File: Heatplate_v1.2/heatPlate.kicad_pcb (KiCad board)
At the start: 2 copper layers, 112 x 180 mm, 62 parts, among them J1 Conn_01x02, J3 TYPE-C-31-M-12, Q1 SS8050, Q2 IRLR8726TRPBF, SW1 SW_Push, SW2 SW_Push, U1 NCP1117-3.3_SOT223, U2 W25Q128JVS, U3 RP2040, U4 FUSB302TMPX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

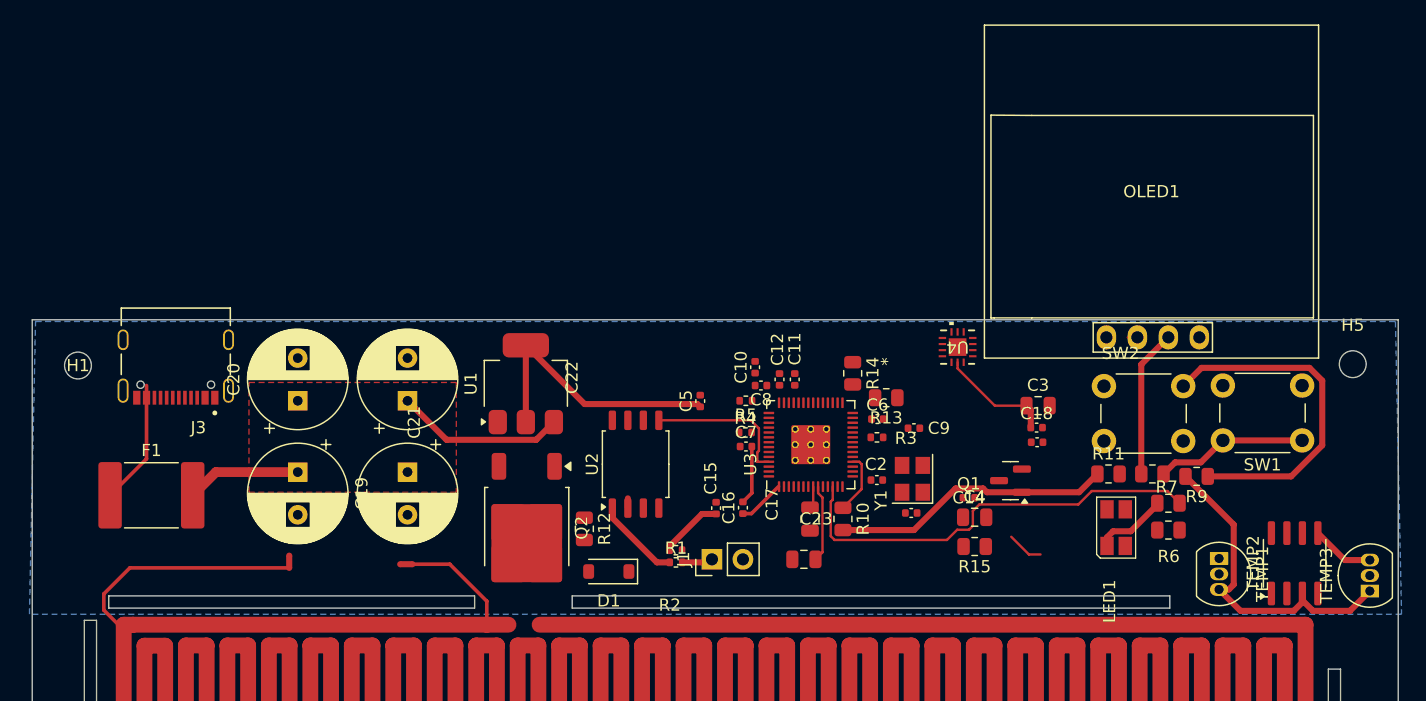
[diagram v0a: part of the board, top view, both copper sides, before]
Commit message: Minor placement changes
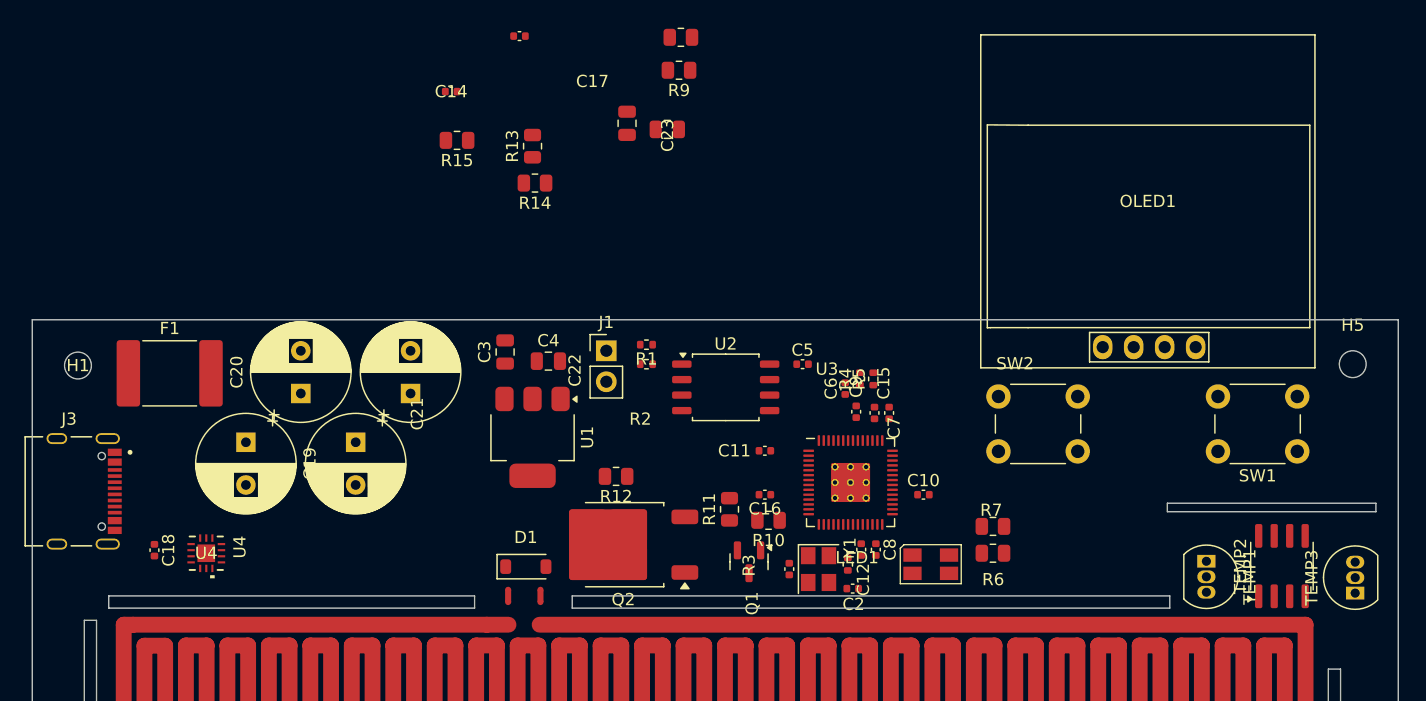
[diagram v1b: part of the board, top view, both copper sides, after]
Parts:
- moved C18 73.0 mm to (71.8, 70.2), turned to -90 degrees
- moved U4 63.9 mm to (76.0, 70.5), turned to -90 degrees
- moved C14 53.9 mm to (96.1, 32.6)
- moved C13 53.9 mm to (101.7, 28.1)
- moved R15 53.9 mm to (96.6, 36.6)
- moved R9 53.9 mm to (114.8, 30.9)
- moved R8 52.7 mm to (114.9, 28.2)
- moved C3 43.9 mm to (100.5, 54.0), turned to 90 degrees
- moved C23 38.6 mm to (110.5, 35.2), turned to 90 degrees
- moved C4 37.2 mm to (104.0, 54.8)
- moved R13 35.6 mm to (102.8, 37.1), turned to 90 degrees
- moved C17 34.0 mm to (113.8, 35.8), turned to 180 degrees
- moved R11 31.2 mm to (118.9, 66.9), turned to 90 degrees
- moved R14 30.4 mm to (103.0, 40.1), turned to 180 degrees
- moved Q1 22.4 mm to (120.5, 71.2), turned to -90 degrees
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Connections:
- net Net-(F1-Pad1) renamed +VDC
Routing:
- net HEATPLATE: track 8744.4 -> 0.00 mm
- net Net-(D1-A): track 0.00 -> 8716.0 mm
- net +3.3V: track 39.7 -> 0.00 mm
- net VBUS: track 35.7 -> 0.00 mm
- net /GPIO9: track 35.7 -> 0.00 mm
- net /GPIO7: track 34.6 -> 0.00 mm
- net +3V3: track 31.7 -> 0.00 mm
- net Net-(Q1-B): track 23.0 -> 0.00 mm
- net /GPIO6: track 14.3 -> 0.00 mm
- net /QSPI_SD0: track 12.2 -> 0.00 mm
- net +VDC: track 10.2 -> 0.00 mm
- net GND: track 10.0 -> 0.00 mm
- net /QSPI_SS: track 7.02 -> 0.00 mm
- net Net-(LED1A-A1): track 6.06 -> 0.00 mm
- net /GPIO15: track 5.03 -> 0.00 mm
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- removed copper zone on B.Cu, net GND
- removed copper zone on F.Cu, net VBUS
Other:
- outline, holes or cut-outs redrawn

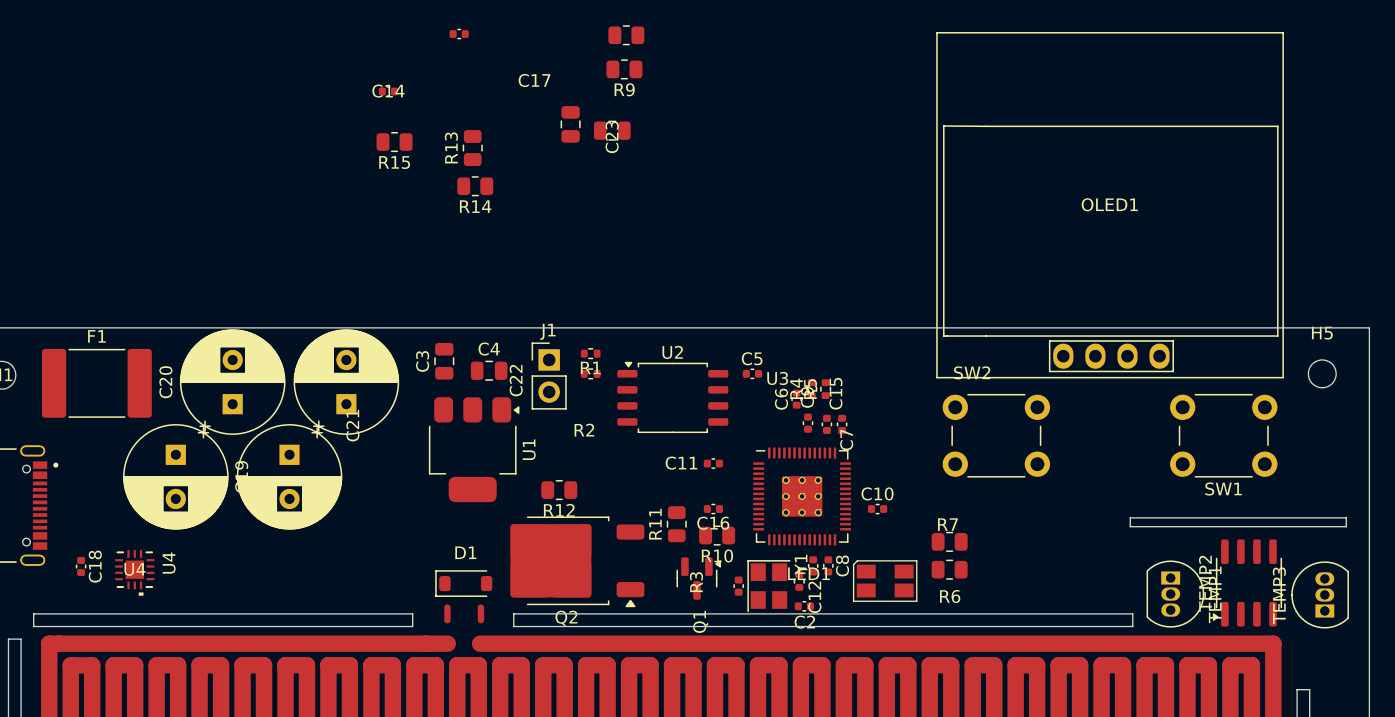
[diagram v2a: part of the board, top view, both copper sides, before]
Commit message: components changed to 0603
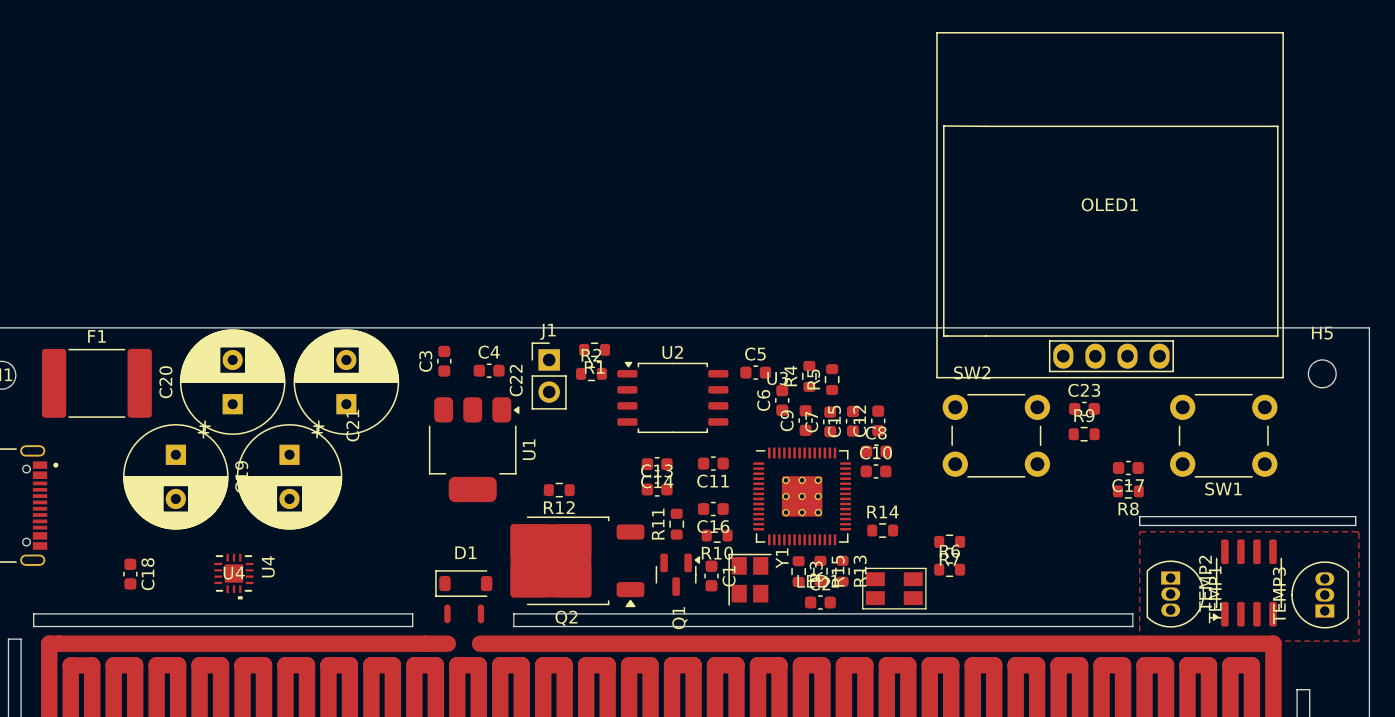
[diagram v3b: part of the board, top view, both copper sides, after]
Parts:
- C1, C10, C11, C12, C13, C14, C15, C16, C18, C2, C5, C6, C7, C8, C9: footprint Capacitor_SMD:C_0402_1005Metric -> Capacitor_SMD:C_0603_1608Metric
- C17, C23, C3, C4: footprint Capacitor_SMD:C_0805_2012Metric -> Capacitor_SMD:C_0603_1608Metric
- R1, R2, R3, R4, R5: footprint Resistor_SMD:R_0402_1005Metric -> Resistor_SMD:R_0603_1608Metric
- R10, R11, R12, R13, R14, R15, R6, R7, R8, R9: footprint Resistor_SMD:R_0805_2012Metric -> Resistor_SMD:R_0603_1608Metric
- moved R8 53.7 mm to (154.7, 64.3)
- moved C17 48.8 mm to (154.7, 62.5)
- moved R15 47.9 mm to (130.3, 70.6), turned to -90 degrees
- moved C23 46.5 mm to (151.2, 57.8), turned to 0 degrees
- moved R9 46.5 mm to (151.2, 59.8), turned to 0 degrees
- moved R13 44.5 mm to (132.0, 70.6), turned to -90 degrees
- moved R14 42.2 mm to (135.2, 67.4), turned to 0 degrees
- moved C13 39.3 mm to (117.3, 64.2)
- moved C14 36.4 mm to (117.3, 62.1)
- moved C12 12.6 mm to (134.8, 58.7), turned to 90 degrees
- moved C8 9.82 mm to (134.7, 61.1), turned to 0 degrees
- moved U4 7.86 mm to (83.8, 70.8)
- moved C18 3.95 mm to (75.7, 70.8)
- moved C10 2.98 mm to (134.7, 62.7)
- moved C1 2.29 mm to (121.7, 71.0)
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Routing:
- added copper zone on F.Cu, net HEATPLATE
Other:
- outline, holes or cut-outs redrawn

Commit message: minor changes
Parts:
- moved R2 0.12 mm to (112.3, 55.0)
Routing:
- net Net-(D1-A): track 8716.0 -> 0.00 mm
- net HEATPLATE: track 0.00 -> 8716.0 mm
- net /GPIO7: track 0.00 -> 6.50 mm
- net Net-(LED1A-A1): track 0.00 -> 6.27 mm
- net Net-(C2-Pad1): track 0.00 -> 5.40 mm
- net Net-(Q1-B): track 0.00 -> 5.02 mm
- net /~{USB_BOOT}: track 0.00 -> 3.11 mm
- net /GPIO18: track 0.00 -> 2.15 mm
- net /GPIO16: track 0.00 -> 1.97 mm
- net /QSPI_SS: track 0.00 -> 1.95 mm
- net /GPIO17: track 0.00 -> 1.91 mm
- net /XOUT: track 0.00 -> 1.72 mm

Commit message: Add files via upload
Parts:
- moved J1 0.17 mm to (108.8, 53.7)
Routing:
- net +3V3: track 0.00 -> 112.1 mm, vias 0 -> 2
- net VBUS: track 0.00 -> 89.6 mm, vias 0 -> 2
- net /D+: track 0.00 -> 72.1 mm, vias 0 -> 2
- net +3.3V: track 0.00 -> 67.7 mm, vias 0 -> 2
- net /QSPI_SS: track 1.95 -> 22.7 mm
- net /cc2: track 0.00 -> 19.7 mm
- net /QSPI_SD2: track 0.00 -> 18.6 mm
- net /QSPI_SD1: track 0.00 -> 14.8 mm
- net Net-(Q1-C): track 0.00 -> 13.6 mm
- net /GPIO6: track 0.00 -> 12.0 mm
- net +1V1: track 0.00 -> 11.0 mm
- net +VDC: track 0.00 -> 8.36 mm
- net /XIN: track 0.00 -> 6.93 mm
- net /GPIO15: track 0.00 -> 5.56 mm
- net Net-(LED1B-A2): track 0.00 -> 4.63 mm
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
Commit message: routing
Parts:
- moved C17 15.7 mm to (170.3, 61.7), turned to 90 degrees
- moved R8 14.1 mm to (168.5, 61.7), turned to 90 degrees
- moved R7 5.34 mm to (135.2, 69.2)
- moved C9 2.65 mm to (131.8, 58.7)
- moved C4 2.56 mm to (101.5, 54.5), turned to 90 degrees
- moved C7 2.45 mm to (133.5, 58.8)
- moved C15 2.40 mm to (135.2, 58.8)
- moved C12 2.15 mm to (137.0, 58.7)
- moved R1 1.99 mm to (110.5, 52.5)
- moved U1 1.95 mm to (101.2, 62.2)
- moved R2 1.92 mm to (110.5, 54.2)
- moved C6 1.92 mm to (127.8, 55.2)
- moved J1 1.80 mm to (107.0, 53.7)
- moved C3 1.58 mm to (99.0, 54.5)
- moved U2 1.41 mm to (118.8, 55.5)
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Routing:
- net +3V3: track 112.1 -> 0.00 mm, vias 2 -> 0
- net VBUS: track 89.6 -> 0.00 mm, vias 2 -> 0
- net /D+: track 72.1 -> 0.00 mm, vias 2 -> 0
- net +3.3V: track 67.7 -> 0.85 mm, vias 2 -> 0
- net /GPIO7: track 6.50 -> 44.2 mm, vias 0 -> 2
- net /GPIO6: track 12.0 -> 49.4 mm, vias 0 -> 2
- net /GPIO21: track 0.00 -> 31.3 mm
- net /GPIO20: track 0.00 -> 28.3 mm
- net /GPIO8: track 0.00 -> 20.4 mm, vias 0 -> 2
- net /cc2: track 19.7 -> 0.00 mm
- net /GPIO9: track 0.00 -> 19.6 mm, vias 0 -> 2
- net Net-(Q1-C): track 13.6 -> 0.00 mm
- net +1V1: track 11.0 -> 0.00 mm
- net /QSPI_SD3: track 0.37 -> 9.74 mm
- net /QSPI_SCLK: track 0.00 -> 8.44 mm
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- added copper zone on B.Cu, net GND

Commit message: routing
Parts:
- moved Y1 0.75 mm to (125.5, 71.5)
- moved R13 0.47 mm to (132.5, 70.6)
- moved R3 0.45 mm to (129.0, 70.7)
- moved C12 0.25 mm to (136.8, 58.7)
- moved C15 0.25 mm to (135.0, 58.8)
- moved C7 0.25 mm to (133.2, 58.8)
- moved C9 0.25 mm to (131.5, 58.7)
- moved R15 0.22 mm to (130.5, 70.6)
- turned TEMP2 to -90 degrees
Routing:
- net /GPIO26_ADC0: track 0.00 -> 63.8 mm, vias 0 -> 1
- net /GPIO5: track 0.00 -> 50.4 mm, vias 0 -> 1
- net /GPIO4: track 0.00 -> 43.7 mm, vias 0 -> 2
- net VBUS: track 0.00 -> 20.8 mm
- net +VDC: track 0.00 -> 10.9 mm
- net /XIN: track 0.00 -> 7.75 mm
- net Net-(D1-A): track 0.00 -> 5.62 mm
- net GND: track 0.00 -> 2.20 mm, vias 0 -> 1
- net /GPIO7: track 44.2 -> 45.0 mm
- net /GPIO6: track 49.4 -> 50.2 mm
- net Net-(C2-Pad1): track 6.12 -> 6.70 mm
- added copper zone on F.Cu, net VBUS

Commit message: routing
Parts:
- moved C18 22.1 mm to (96.0, 62.2)
- moved R6 3.25 mm to (143.8, 70.5)
- moved LED1 2.12 mm to (138.2, 72.0)
- moved R7 1.50 mm to (136.8, 69.2)
- moved C2 0.76 mm to (129.8, 73.0)
- moved C11 0.45 mm to (122.2, 62.1)
- turned C14 to 0 degrees
- turned U4 to 90 degrees
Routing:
- net /D-: track 0.00 -> 72.1 mm, vias 0 -> 2
- net /D+: track 0.00 -> 69.9 mm, vias 0 -> 2
- net +3V3: track 0.00 -> 64.7 mm, vias 0 -> 3
- net /GPIO18: track 2.25 -> 58.0 mm, vias 0 -> 2
- net /GPIO16: track 1.97 -> 55.1 mm, vias 0 -> 2
- net /GPIO17: track 1.91 -> 54.7 mm, vias 0 -> 2
- net VBUS: track 20.8 -> 70.5 mm
- net GND: track 2.20 -> 44.4 mm, vias 1 -> 4
- net /cc1: track 0.00 -> 17.5 mm
- net /cc2: track 0.00 -> 16.9 mm
- net Net-(Q1-C): track 0.00 -> 14.3 mm
- net +3.3V: track 0.50 -> 9.07 mm
- net +VDC: track 10.9 -> 17.4 mm
- net Net-(Q1-B): track 0.00 -> 5.02 mm
- net /QSPI_SS: track 22.0 -> 26.4 mm
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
